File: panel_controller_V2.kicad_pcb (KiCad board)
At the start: 2 copper layers, 153.2 x 105.2 mm, 18 parts, among them J1 Screw_Terminal_01x02, J2 Screw_Terminal_01x04, J3 SSW-104-01-F-S, J4 SSW-108-02-G-D, J5 Screw_Terminal_01x03, U1 ESP32-DEVKIT-V1, U2 RA-02_LORA

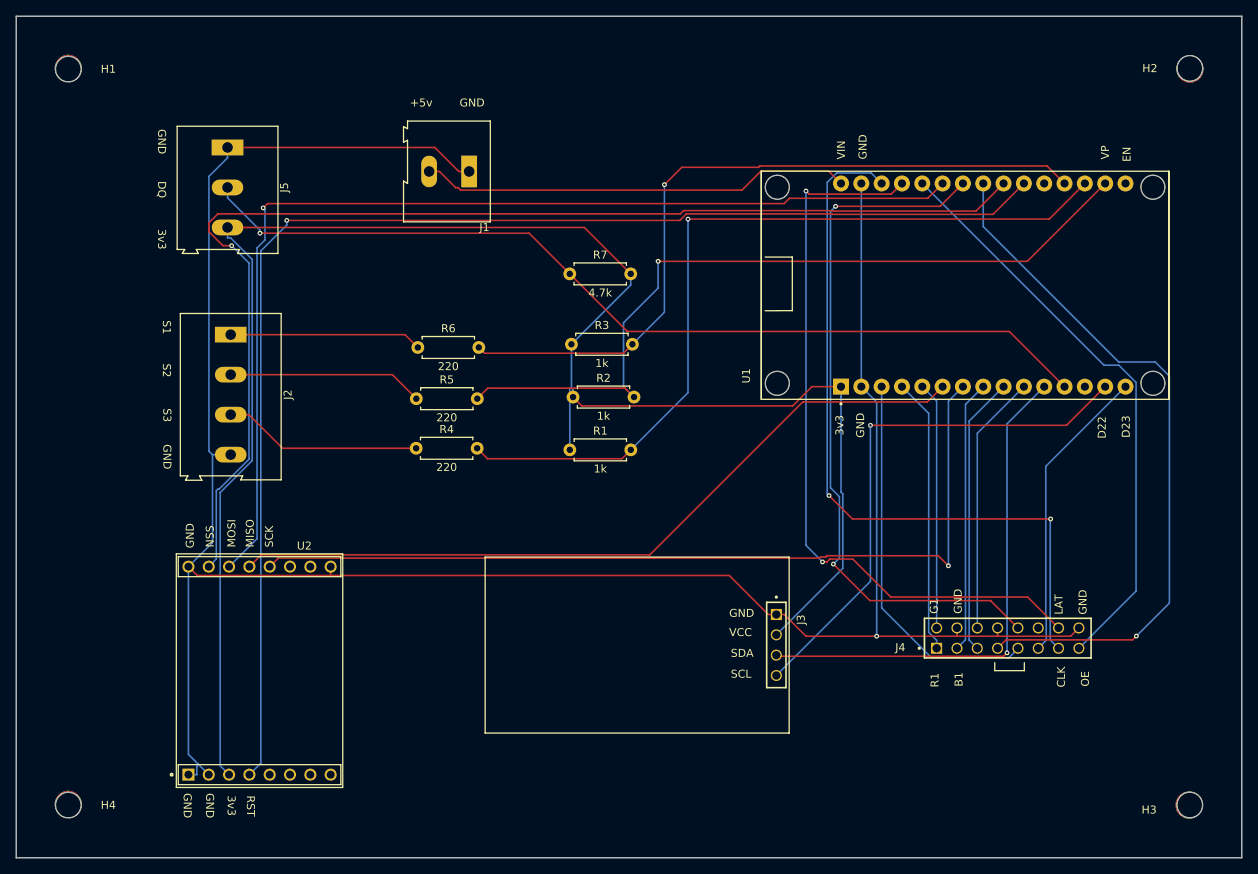
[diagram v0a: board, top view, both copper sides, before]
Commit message: headers parallel to esp32 added
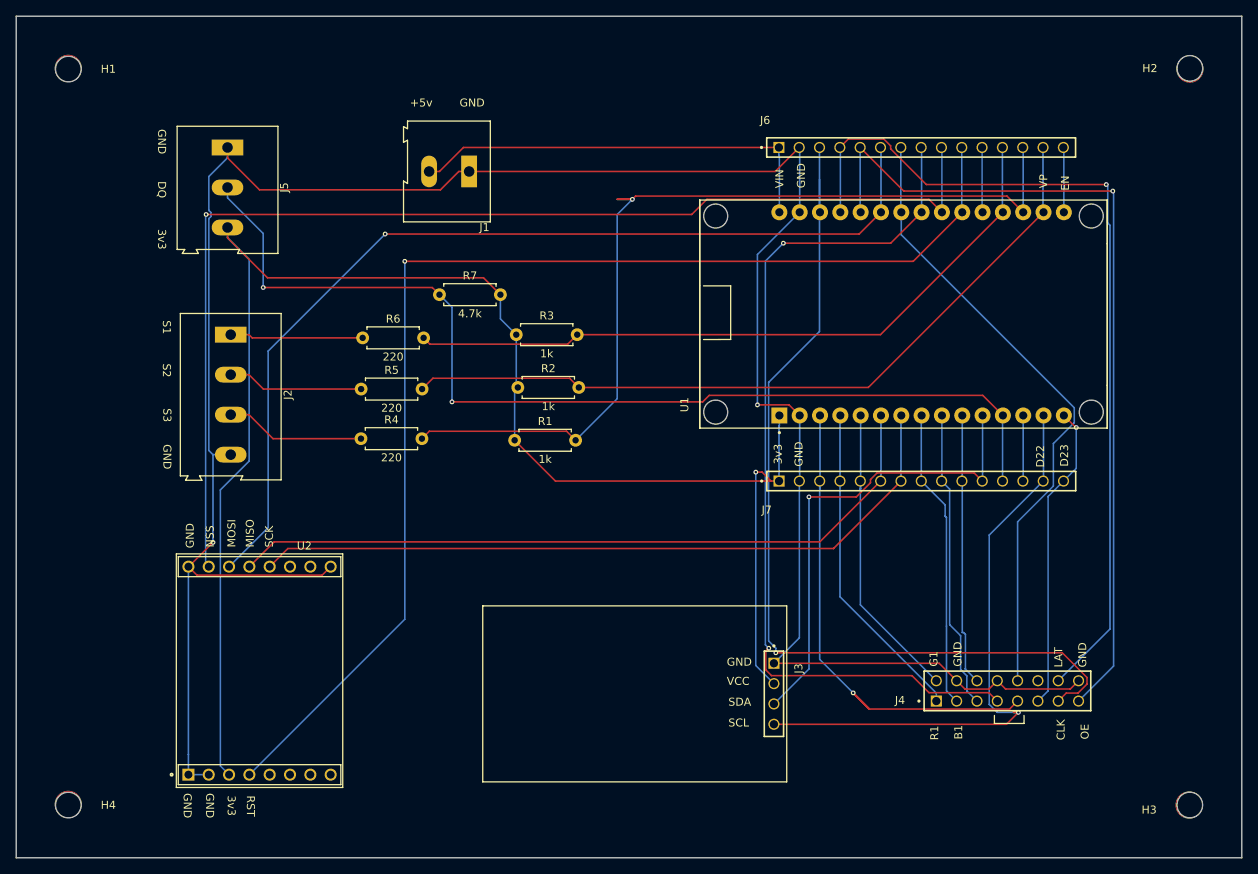
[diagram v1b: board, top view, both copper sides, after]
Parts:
- added J6: SSW-115-01-F-S, SSW_115_01_F_S:SAMTEC_SSW-115-01-F-S, F.Cu at (165.1, 75.6)
- added J7: SSW-115-01-F-S, SSW_115_01_F_S:SAMTEC_SSW-115-01-F-S, F.Cu at (165.1, 117.3)
- moved R7 16.5 mm to (122.7, 94.0)
- moved U1 8.50 mm to (180.7, 96.4)
- moved R1 7.00 mm to (132.1, 112.2)
- moved R3 7.00 mm to (132.3, 99.0)
- moved R4 7.00 mm to (112.9, 112.0)
- moved R5 7.00 mm to (112.9, 105.8)
- moved R6 7.00 mm to (113.1, 99.4)
- moved R2 7.00 mm to (132.5, 105.6)
- moved J4 6.60 mm to (194.8, 134.8)
- moved J3 6.11 mm to (173.0, 142.9)
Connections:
- U1 pad 13: unconnected-(U1-TX0-Pad13) -> Net-(U1-TX0)
- U1 pad 16: unconnected-(U1-EN-Pad16) -> Net-(U1-EN)
- U1 pad 20: unconnected-(U1-D35-Pad20) -> Net-(U1-D35)
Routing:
- net Net-(U1-D14): track 73.2 -> 108.0 mm, vias 0 -> 1
- net Net-(U1-D25): track 88.6 -> 114.2 mm, vias 1 -> 2
- net Net-(U1-D13): track 92.6 -> 115.8 mm, vias 2 -> 1
- net Net-(U1-D15): track 47.8 -> 70.6 mm, vias 0 -> 1
- net +3V3: track 220.8 -> 202.2 mm, vias 0 -> 1
- net Net-(U1-TX2): track 109.1 -> 91.6 mm, vias 1 -> 0
- net Net-(U1-D12): track 93.1 -> 110.1 mm, vias 2 -> 1
- net Net-(U1-VN): track 103.5 -> 118.7 mm
- net Net-(J5-Pin_2): track 115.9 -> 129.3 mm, vias 1 -> 2
- net Net-(U1-D32): track 165.3 -> 152.6 mm
- net Net-(U1-D27): track 133.0 -> 120.9 mm
- net Net-(U1-D26): track 89.2 -> 78.6 mm, vias 2 -> 0
- net Net-(U1-D22): track 67.5 -> 76.6 mm
- net Net-(U1-TX0): track 0.00 -> 8.22 mm
- net Net-(U1-EN): track 0.00 -> 8.12 mm
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
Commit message: Ignore .history and DS_Store, cleanup project
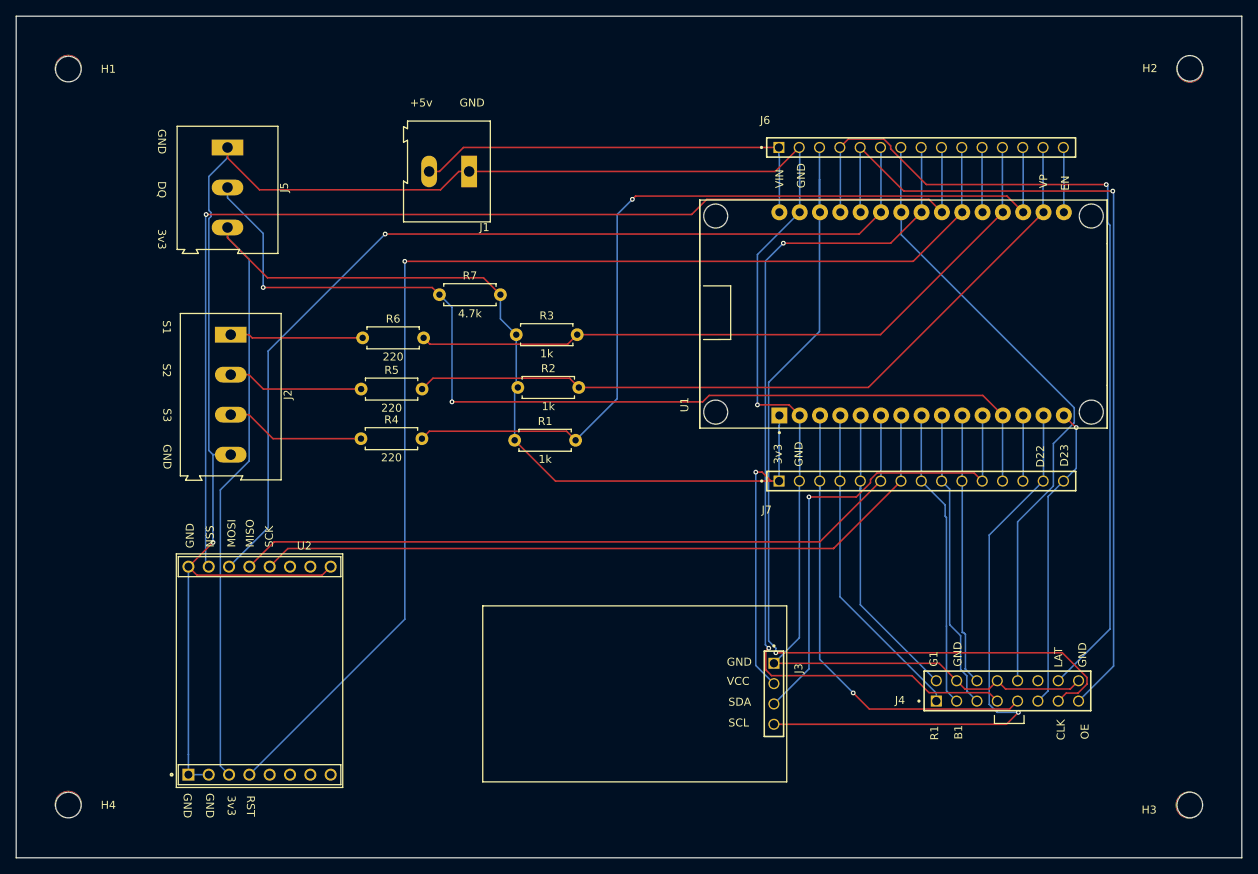
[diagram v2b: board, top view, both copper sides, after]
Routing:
- net Net-(U1-D15): track 70.6 -> 59.2 mm
- net Net-(U1-VN): track 118.7 -> 111.1 mm
- net Net-(U1-D22): track 76.6 -> 74.2 mm
- net Net-(U1-D25): track 114.2 -> 112.2 mm
- net GND: track 296.0 -> 294.3 mm
- net Net-(U1-D23): track 39.1 -> 38.3 mm
- net Net-(U1-D12): track 110.1 -> 109.5 mm

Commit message: Removed copper ring on NPTH and clean
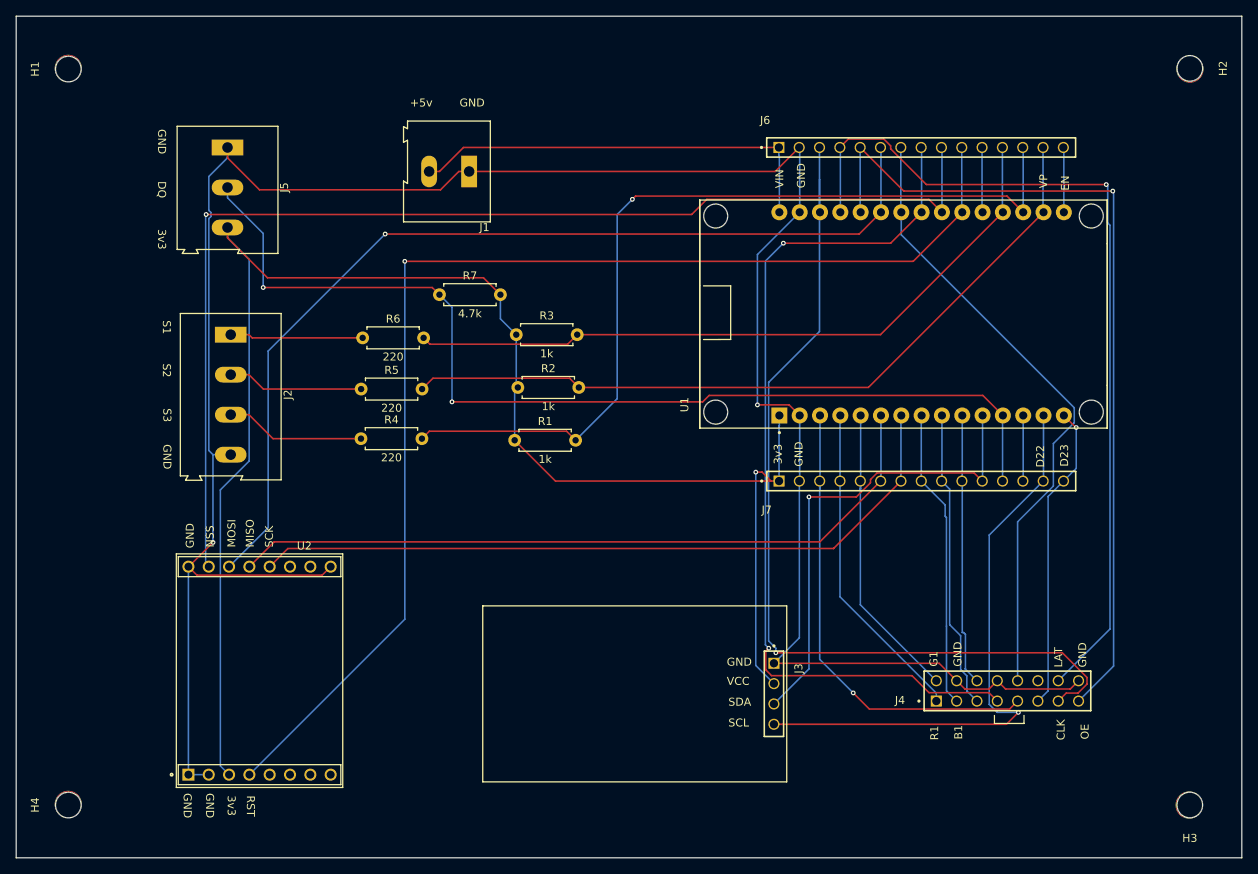
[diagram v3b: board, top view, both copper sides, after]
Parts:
- H1, H2, H3, H4: value MountingHole_3.2mm_M3 -> 3.2mm_M3_NR; footprint MountingHole:MountingHole_3.2mm_M3 -> Mounting Hole:3.2mm_M3_NR
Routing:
- net +3V3: track 202.2 -> 201.4 mm
- net GND: track 294.3 -> 293.5 mm
- net Net-(U1-D33): track 145.9 -> 145.3 mm
